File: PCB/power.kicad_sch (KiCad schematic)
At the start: 2 parts, among them J1 Screw_Terminal_01x02

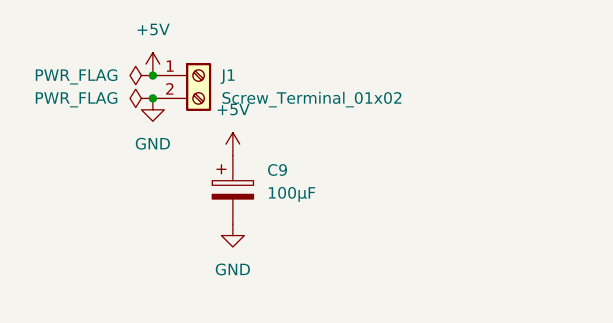
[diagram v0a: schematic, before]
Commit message: refactor: Update PCB with power jumper
This adds a jumper to connect the digital and analog pins to either 3.3v or 5v depending on the jumper position.
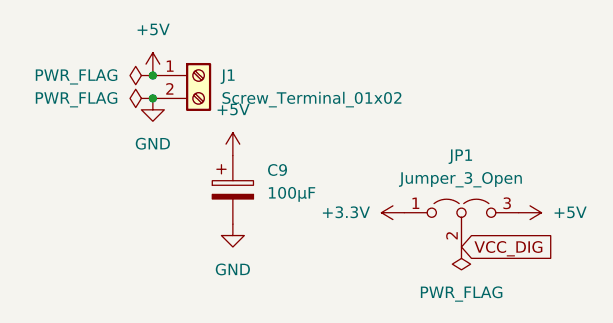
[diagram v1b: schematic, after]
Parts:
- added JP1: Jumper_3_Open, Connector_PinHeader_2.54mm:PinHeader_1x03_P2.54mm_Vertical, symbol Jumper:Jumper_3_Open
- J1: now left out of the parts list
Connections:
- net +5V: now also JP1.3 (B)
- new net +3.3V: JP1.1 (A)
- new net VCC_DIG: JP1.2 (C)
